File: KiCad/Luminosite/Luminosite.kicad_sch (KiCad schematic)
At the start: 12 parts, among them J1 Conn_01x03, U1 MCP6022

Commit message: Capteur de température
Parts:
- removed C1: 10p, symbol Device:C_Small
- removed C2: 100n, symbol Device:C_Small
- removed C3: 220n, symbol Device:C_Small
- removed D2: D_Photo, symbol Device:D_Photo
- removed J1: Conn_01x03, symbol Connector_Generic:Conn_01x03
- removed R1: 68k, symbol Device:R_Small
- removed R2: 100k, symbol Device:R_Small
- removed R3, R4, R5, R6: 10k, symbol Device:R_Small
- removed U1: MCP6022, symbol Amplifier_Operational:MCP6022
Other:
- added sheet Luminosité (Capteur_luminosite.kicad_sch)
- added sheet Température (Capteur_temperature.kicad_sch)

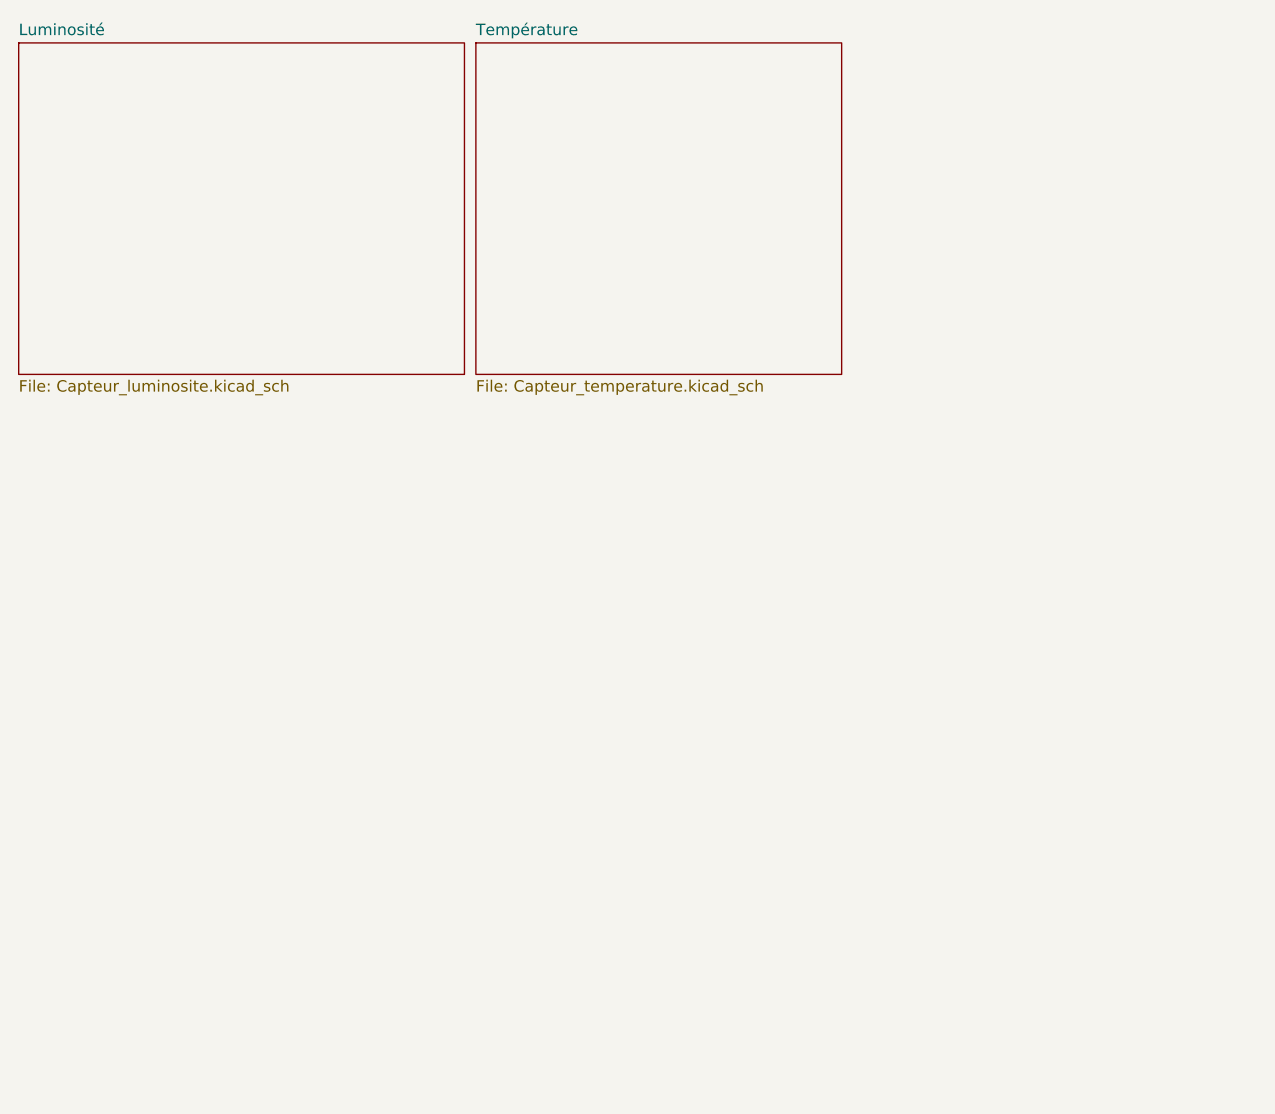
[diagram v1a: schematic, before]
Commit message: Ajout du Schéma Pompe
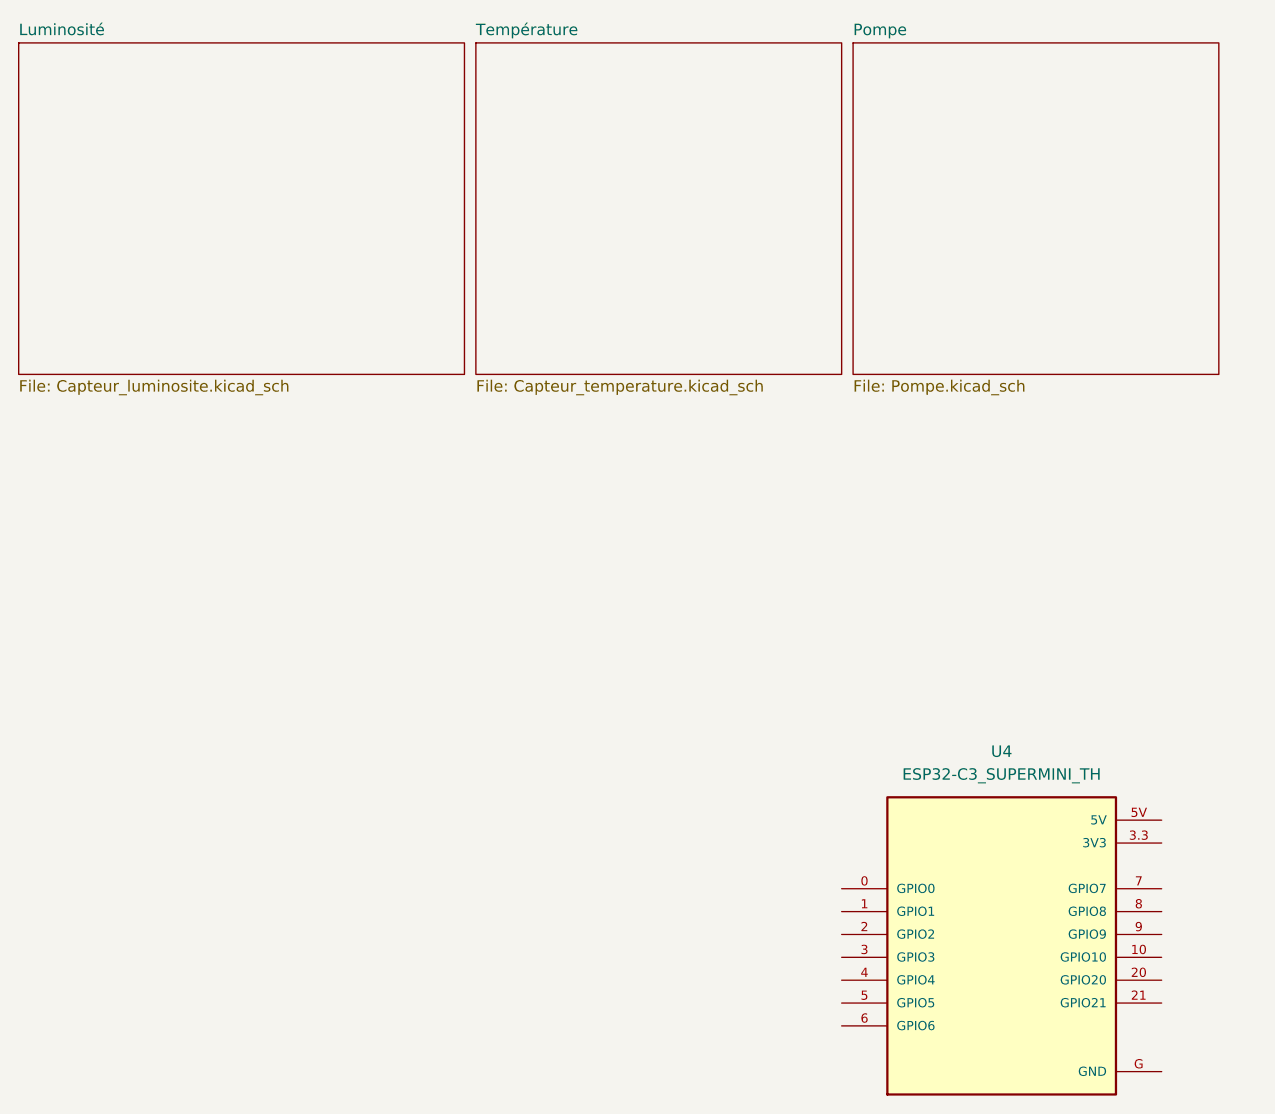
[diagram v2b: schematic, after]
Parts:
- added U4: ESP32-C3_SUPERMINI_TH, ESP32-C3_SUPERMINI_TH:MODULE_ESP32-C3_SUPERMINI_TH, symbol ESP32-C3-Supermini:ESP32-C3_SUPERMINI_TH
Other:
- added sheet Pompe (Pompe.kicad_sch)
